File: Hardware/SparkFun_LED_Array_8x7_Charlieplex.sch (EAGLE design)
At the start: 73 parts

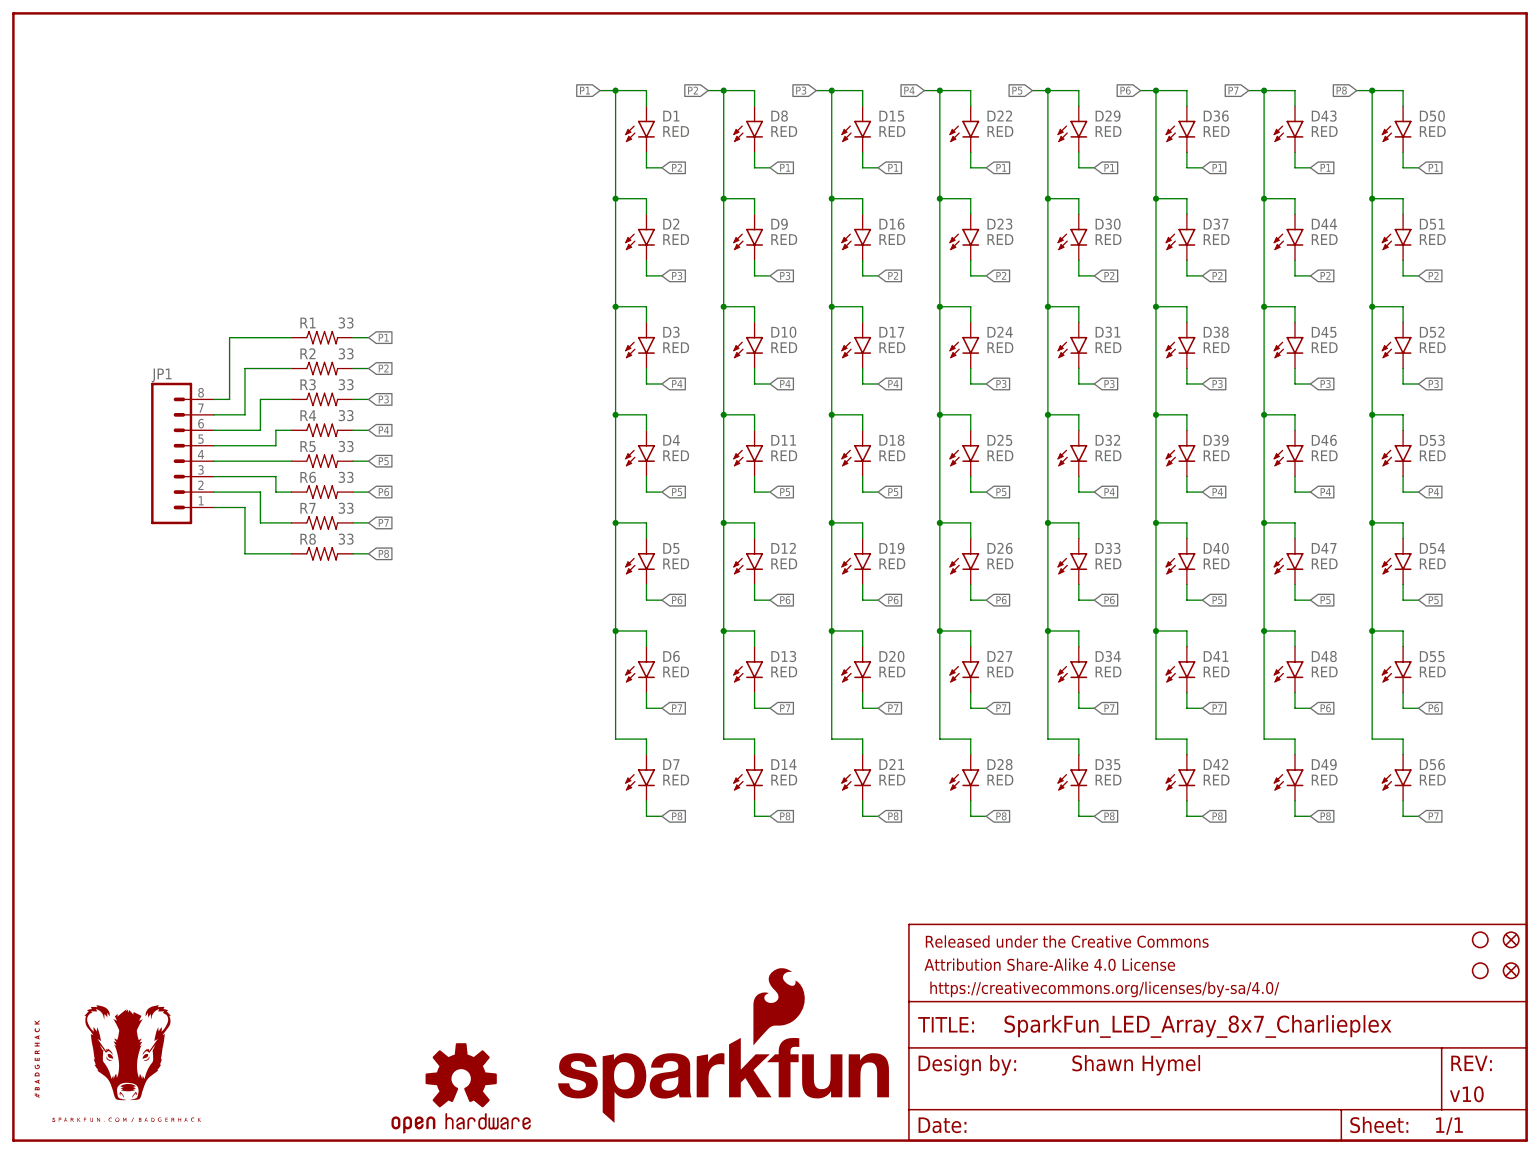
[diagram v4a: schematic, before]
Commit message: Changed pin numbers to letters (A-H). Changed revision to v11.
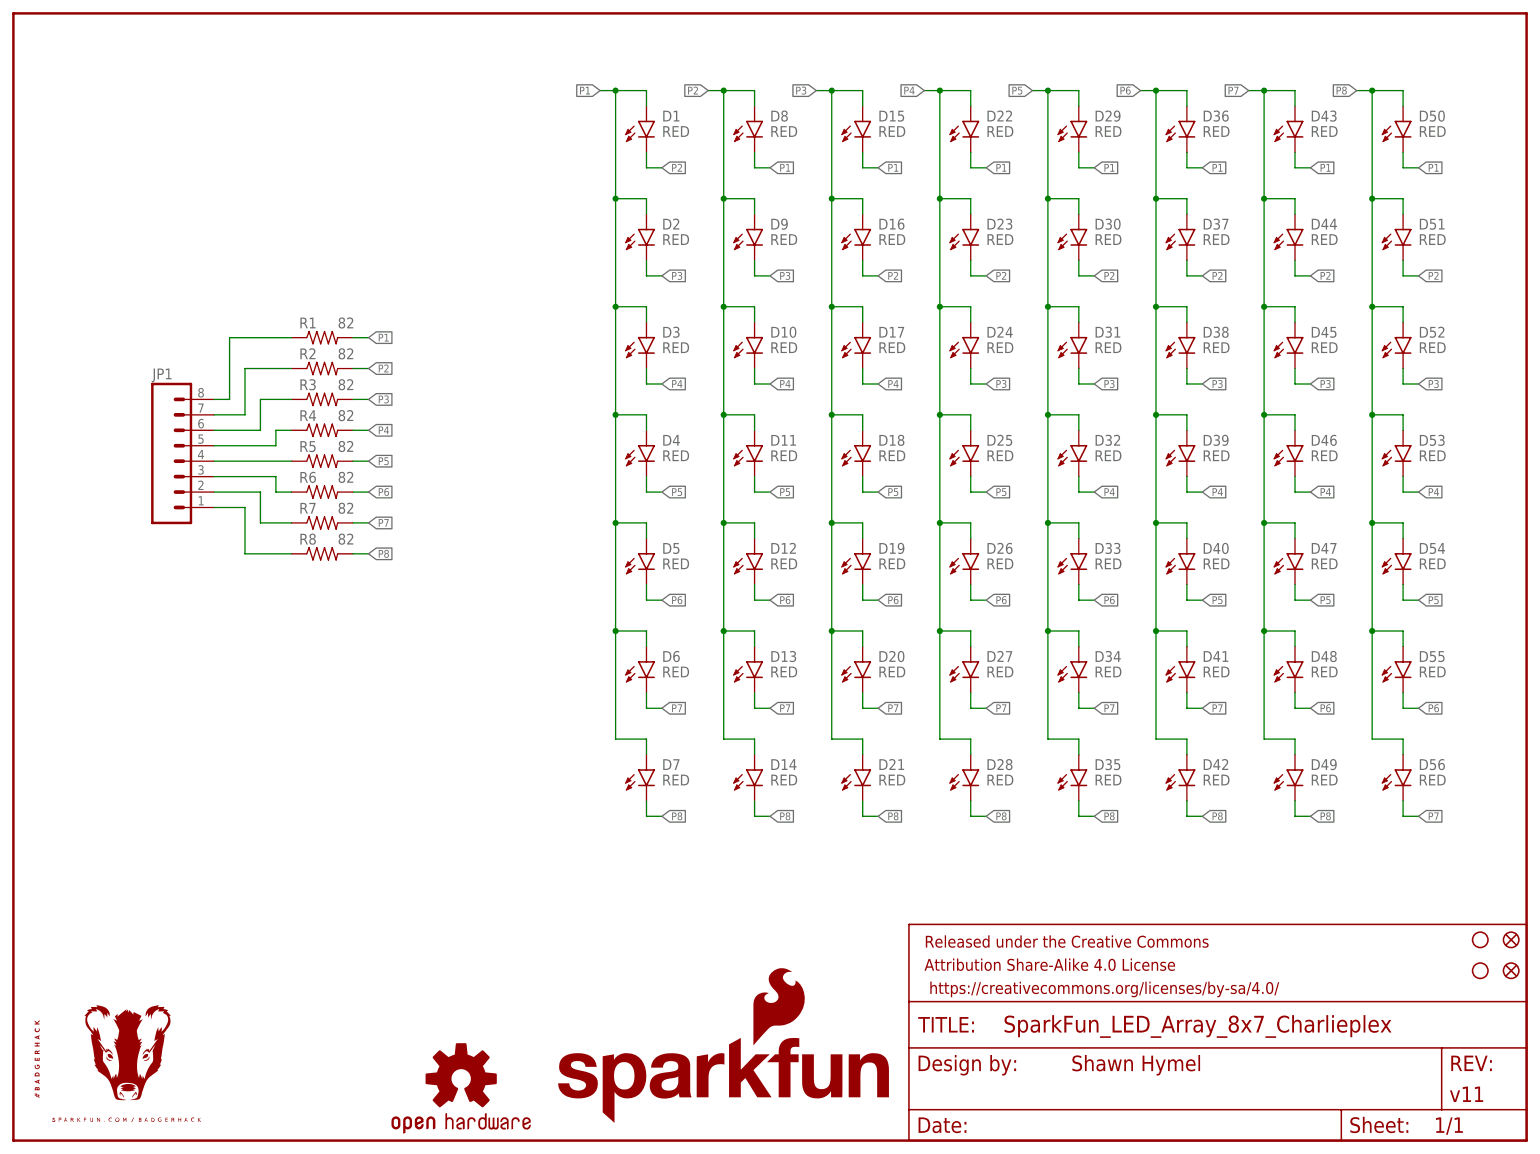
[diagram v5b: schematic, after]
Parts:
- FRAME1: VERSION v10 -> v11
- R1, R2, R3, R4, R5, R6, R7, R8: value 33 -> 82; device SparkFun-Resistors:RESISTOR0603-RES -> SparkFun-Resistors:82OHM-1/10W-1%(0603)SMD; PROD_ID RES-08270 -> (none)
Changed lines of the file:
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@@
 <layer number="223" name="223bmp" color="24" fill="1" visible="no" active="no"/>
 <layer number="224" name="224bmp" color="25" fill="1" visible="no" active="no"/>
+<layer number="225" name="225bmp" color="7" fill="1" visible="yes" active="yes"/>
+<layer number="226" name="226bmp" color="7" fill="1" visible="yes" active="yes"/>
+<layer number="227" name="227bmp" color="7" fill="1" visible="yes" active="yes"/>
+<layer number="228" name="228bmp" color="7" fill="1" visible="yes" active="yes"/>
+<layer number="229" name="229bmp" color="7" fill="1" visible="yes" active="yes"/>
+<layer number="230" name="230bmp" color="7" fill="1" visible="yes" active="yes"/>
+<layer number="231" name="231bmp" color="7" fill="1" visible="yes" active="yes"/>
 <layer number="248" name="Housing" color="7" fill="1" visible="yes" active="yes"/>
 <layer number="249" name="Edge" color="7" fill="1" visible="yes" active="yes"/>
@@
 <part name="FRAME1" library="SparkFun-Aesthetics" deviceset="FRAME-LETTER" device="">
 <attribute name="DESIGNER" value="Shawn Hymel"/>
-<attribute name="VERSION" value="v10"/>
+<attribute name="VERSION" value="v11"/>
 </part>
-<part name="R1" library="SparkFun-Resistors" deviceset="RESISTOR" device="0603-RES" value="33">
-<attribute name="PROD_ID" value="RES-08270"/>
-</part>
+<part name="R1" library="SparkFun-Resistors" deviceset="82OHM-1/10W-1%(0603)" device="SMD" value="82"/>
 <part name="D1" library="SparkFun-LED" deviceset="LED-RED" device="0603" value="RED"/>
 <part name="D2" library="SparkFun-LED" deviceset="LED-RED" device="0603" value="RED"/>
@@
 <part name="D55" library="SparkFun-LED" deviceset="LED-RED" device="0603" value="RED"/>
 <part name="D56" library="SparkFun-LED" deviceset="LED-RED" device="0603" value="RED"/>
-<part name="R2" library="SparkFun-Resistors" deviceset="RESISTOR" device="0603-RES" value="33">
-<attribute name="PROD_ID" value="RES-08270"/>
-</part>
-<part name="R3" library="SparkFun-Resistors" deviceset="RESISTOR" device="0603-RES" value="33">
-<attribute name="PROD_ID" value="RES-08270"/>
-</part>
-<part name="R4" library="SparkFun-Resistors" deviceset="RESISTOR" device="0603-RES" value="33">
-<attribute name="PROD_ID" value="RES-08270"/>
-</part>
-<part name="R5" library="SparkFun-Resistors" deviceset="RESISTOR" device="0603-RES" value="33">
-<attribute name="PROD_ID" value="RES-08270"/>
-</part>
-<part name="R6" library="SparkFun-Resistors" deviceset="RESISTOR" device="0603-RES" value="33">
-<attribute name="PROD_ID" value="RES-08270"/>
-</part>
-<part name="R7" library="SparkFun-Resistors" deviceset="RESISTOR" device="0603-RES" value="33">
-<attribute name="PROD_ID" value="RES-08270"/>
-</part>
-<part name="R8" library="SparkFun-Resistors" deviceset="RESISTOR" device="0603-RES" value="33">
-<attribute name="PROD_ID" value="RES-08270"/>
-</part>
+<part name="R2" library="SparkFun-Resistors" deviceset="82OHM-1/10W-1%(0603)" device="SMD" value="82"/>
+<part name="R3" library="SparkFun-Resistors" deviceset="82OHM-1/10W-1%(0603)" device="SMD" value="82"/>
+<part name="R4" library="SparkFun-Resistors" deviceset="82OHM-1/10W-1%(0603)" device="SMD" value="82"/>
+<part name="R5" library="SparkFun-Resistors" deviceset="82OHM-1/10W-1%(0603)" device="SMD" value="82"/>
+<part name="R6" library="SparkFun-Resistors" deviceset="82OHM-1/10W-1%(0603)" device="SMD" value="82"/>
+<part name="R7" library="SparkFun-Resistors" deviceset="82OHM-1/10W-1%(0603)" device="SMD" value="82"/>
+<part name="R8" library="SparkFun-Resistors" deviceset="82OHM-1/10W-1%(0603)" device="SMD" value="82"/>
 <part name="FID1" library="SparkFun-Aesthetics" deviceset="FIDUCIAL" device="1X2"/>
 <part name="FID2" library="SparkFun-Aesthetics" deviceset="FIDUCIAL" device="1X2"/>

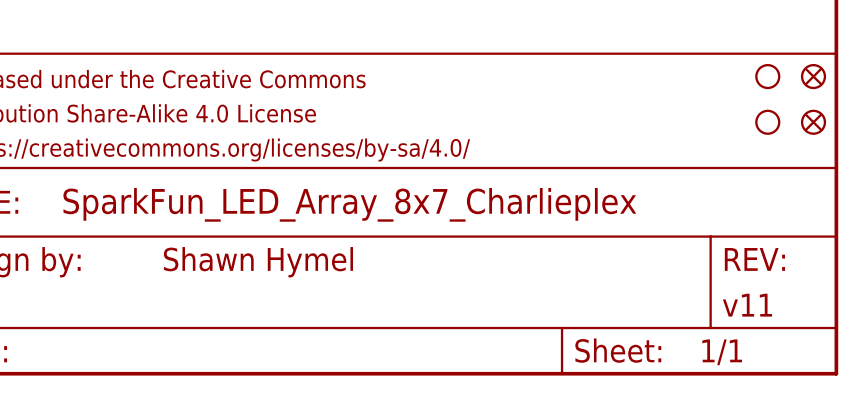
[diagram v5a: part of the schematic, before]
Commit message: Swapped resistors for 82 Ohm. Made link and hashtag larger on silk.
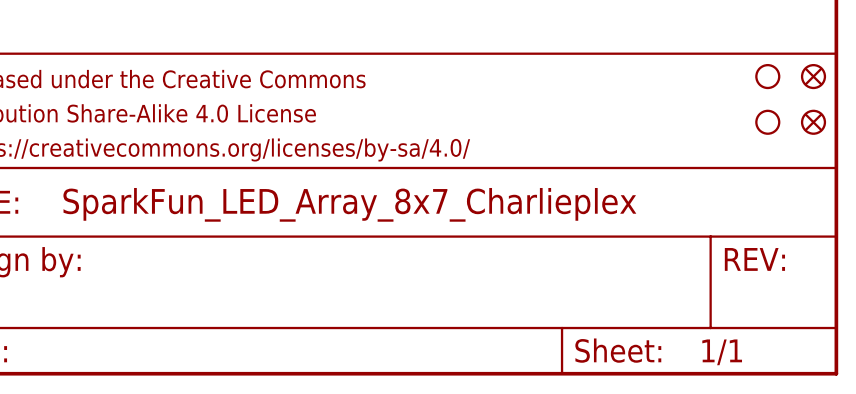
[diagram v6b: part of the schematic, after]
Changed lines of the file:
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@@
 <layer number="56" name="wert" color="7" fill="1" visible="no" active="no"/>
 <layer number="57" name="tCAD" color="7" fill="1" visible="no" active="no"/>
+<layer number="59" name="tCarbon" color="7" fill="1" visible="no" active="no"/>
+<layer number="60" name="bCarbon" color="7" fill="1" visible="no" active="no"/>
 <layer number="90" name="Modules" color="5" fill="1" visible="yes" active="yes"/>
 <layer number="91" name="Nets" color="2" fill="1" visible="yes" active="yes"/>
@@
 <layer number="127" name="_tValues" color="7" fill="1" visible="yes" active="yes"/>
 <layer number="128" name="_bValues" color="7" fill="1" visible="yes" active="yes"/>
+<layer number="129" name="Mask" color="7" fill="1" visible="yes" active="yes"/>
 <layer number="131" name="tAdjust" color="7" fill="1" visible="yes" active="yes"/>
 <layer number="132" name="bAdjust" color="7" fill="1" visible="yes" active="yes"/>

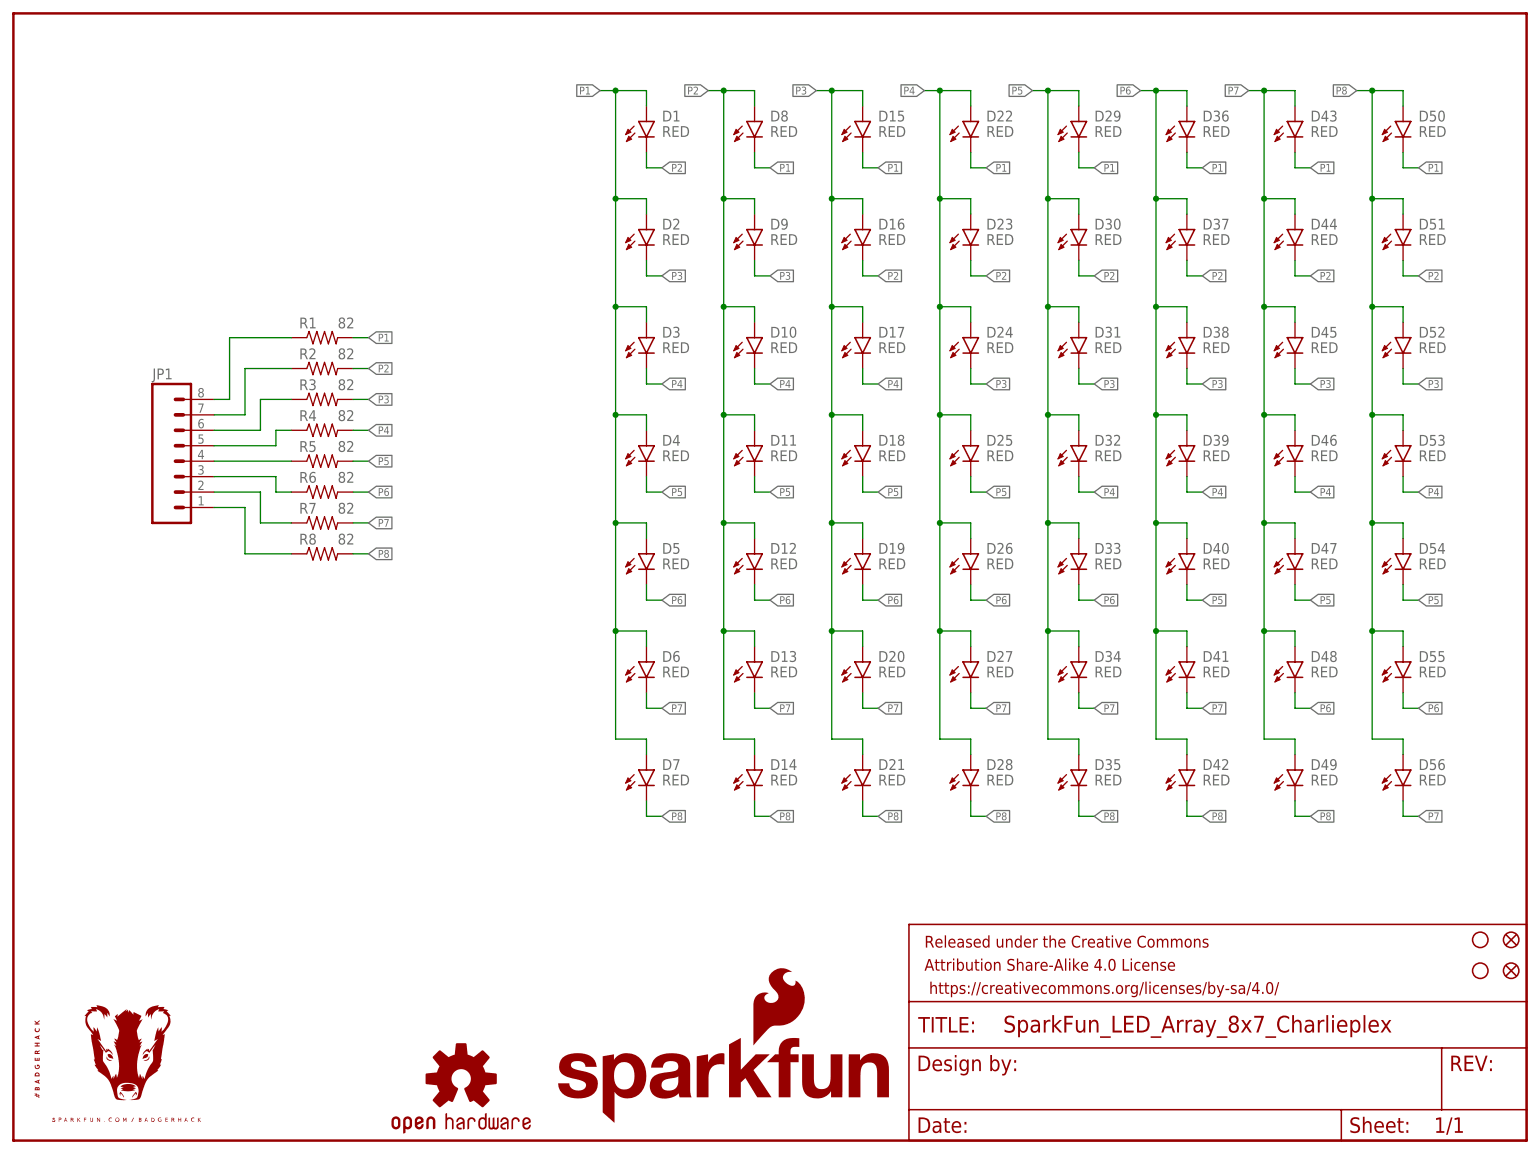
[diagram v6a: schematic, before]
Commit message: Added name and version to schematic. Added info text A-H on pins in schematic.
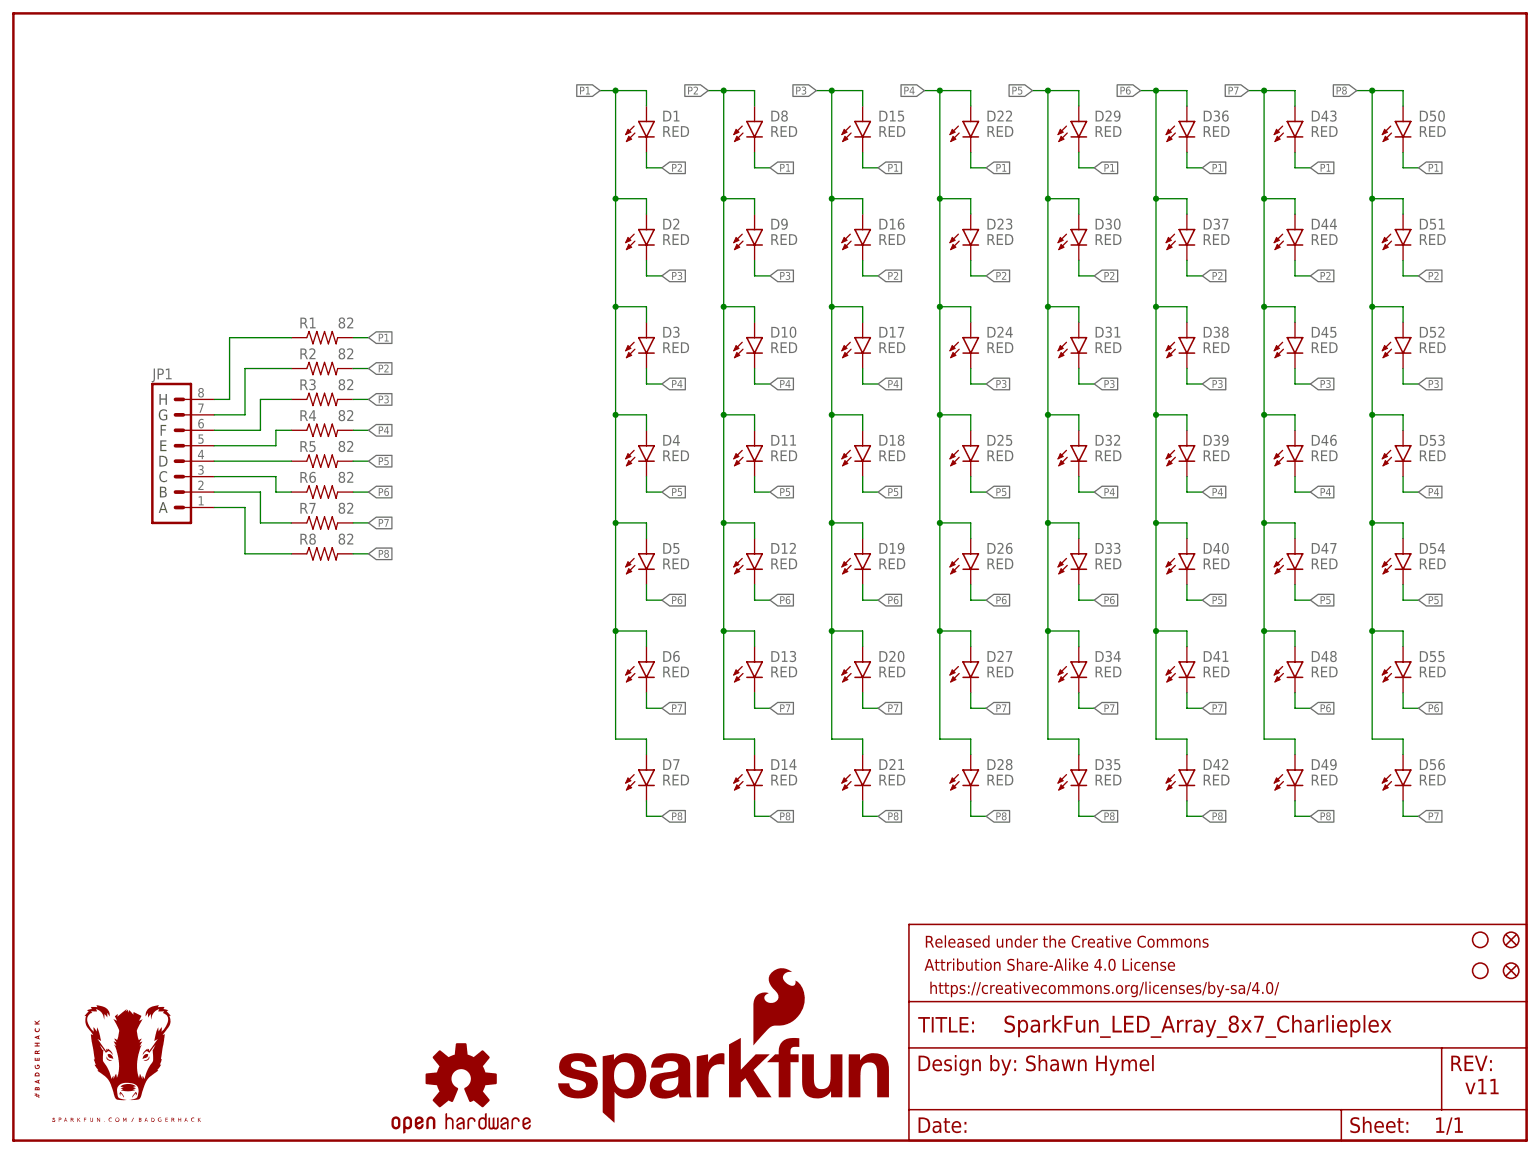
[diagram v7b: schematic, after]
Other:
- note added: "A"
- note added: "B"
- note added: "C"
- note added: "D"
- note added: "E"
- note added: "F"
- note added: "G"
- note added: "H"
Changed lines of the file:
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@@
 <setting verticaltext="up"/>
 </settings>
-<grid distance="0.1" unitdist="inch" unit="inch" style="lines" multiple="1" display="no" altdistance="0.01" altunitdist="inch" altunit="inch"/>
+<grid distance="0.1" unitdist="inch" unit="inch" style="lines" multiple="1" display="yes" altdistance="0.01" altunitdist="inch" altunit="inch"/>
 <layers>
 <layer number="1" name="Top" color="4" fill="1" visible="no" active="no"/>
@@
 <sheet>
 <plain>
+<text x="24.638" y="104.14" size="1.778" layer="97" align="center">A</text>
+<text x="24.638" y="106.68" size="1.778" layer="97" align="center">B</text>
+<text x="24.638" y="109.22" size="1.778" layer="97" align="center">C</text>
+<text x="24.638" y="111.76" size="1.778" layer="97" align="center">D</text>
+<text x="24.638" y="114.3" size="1.778" layer="97" align="center">E</text>
+<text x="24.638" y="116.84" size="1.778" layer="97" align="center">F</text>
+<text x="24.638" y="119.38" size="1.778" layer="97" align="center">G</text>
+<text x="24.638" y="121.92" size="1.778" layer="97" align="center">H</text>
 </plain>
 <instances>
-<instance part="FRAME1" gate="G$1" x="0" y="0"/>
+<instance part="FRAME1" gate="G$1" x="0" y="0">
+<attribute name="DESIGNER" x="166.37" y="11.43" size="2.54" layer="94"/>
+<attribute name="VERSION" x="238.76" y="7.62" size="2.54" layer="94"/>
+</instance>
 <instance part="FRAME1" gate="V" x="147.32" y="0"/>
 <instance part="R1" gate="G$1" x="50.8" y="132.08" smashed="yes">
